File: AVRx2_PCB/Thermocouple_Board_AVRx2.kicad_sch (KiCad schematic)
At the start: 78 parts, among them J6 UPDI-1, Q1 DMN2310U, U11 STS40-CD1B, U12 ADS1246IPWR, U2 ATtiny1604-SS, U3 H11L1, U4 AP2112K-3.3, U5 AP2112K-3.3, U6 TSZ121, U7 MCP1501T-20E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

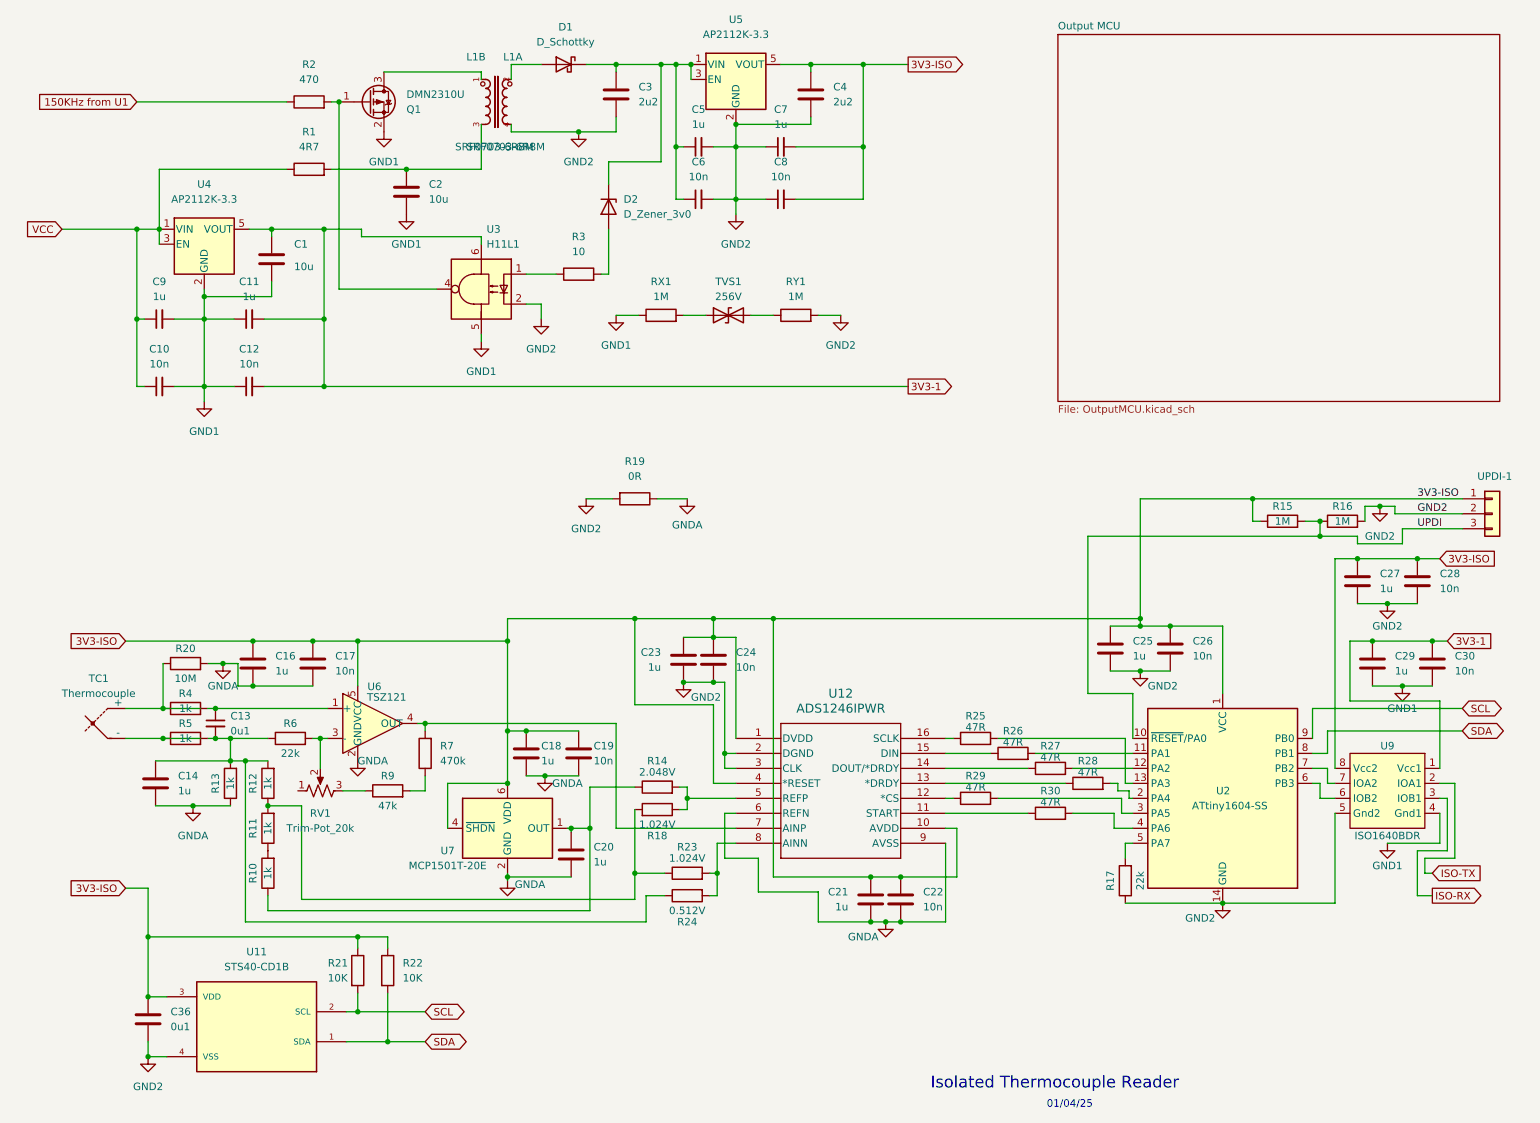
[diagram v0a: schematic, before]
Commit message: Fix a couple of switched traces
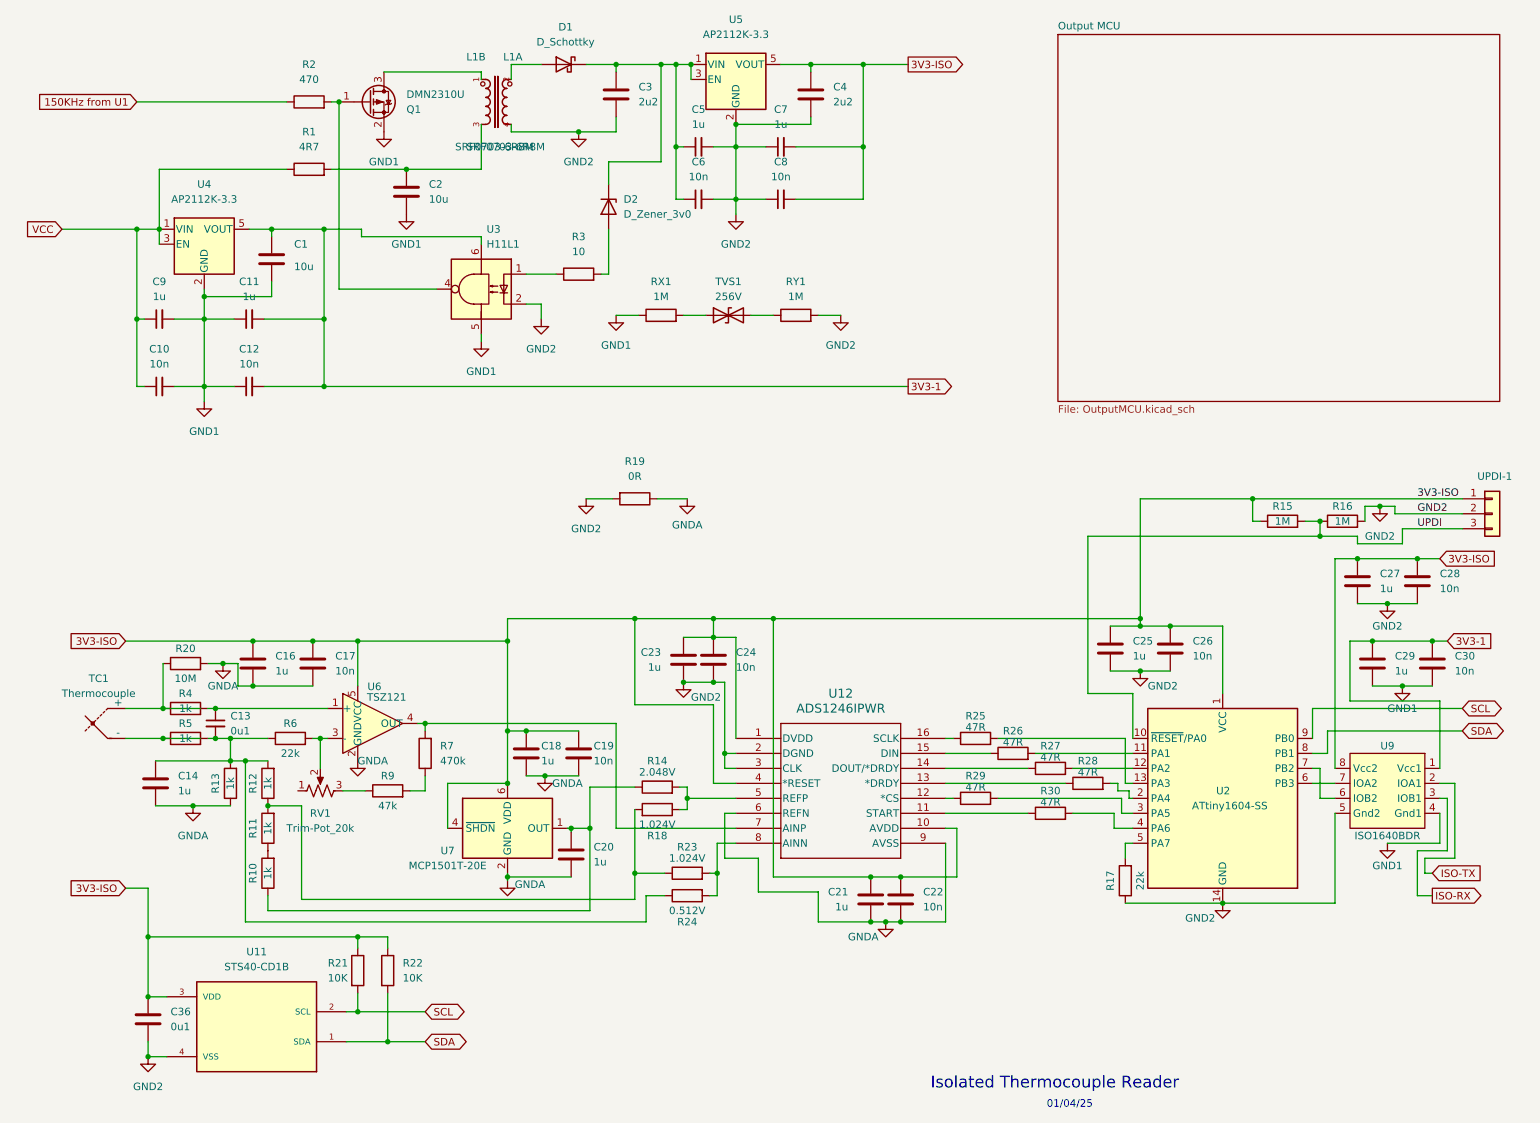
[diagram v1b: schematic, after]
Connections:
- net at U2.6 (PB3): now also U9.7 (IOA2); no longer U9.6 (IOB2)
- net at U2.7 (PB2): now also U9.6 (IOB2); no longer U9.7 (IOA2)

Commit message: Fix crossed traces that were found during prototype testing
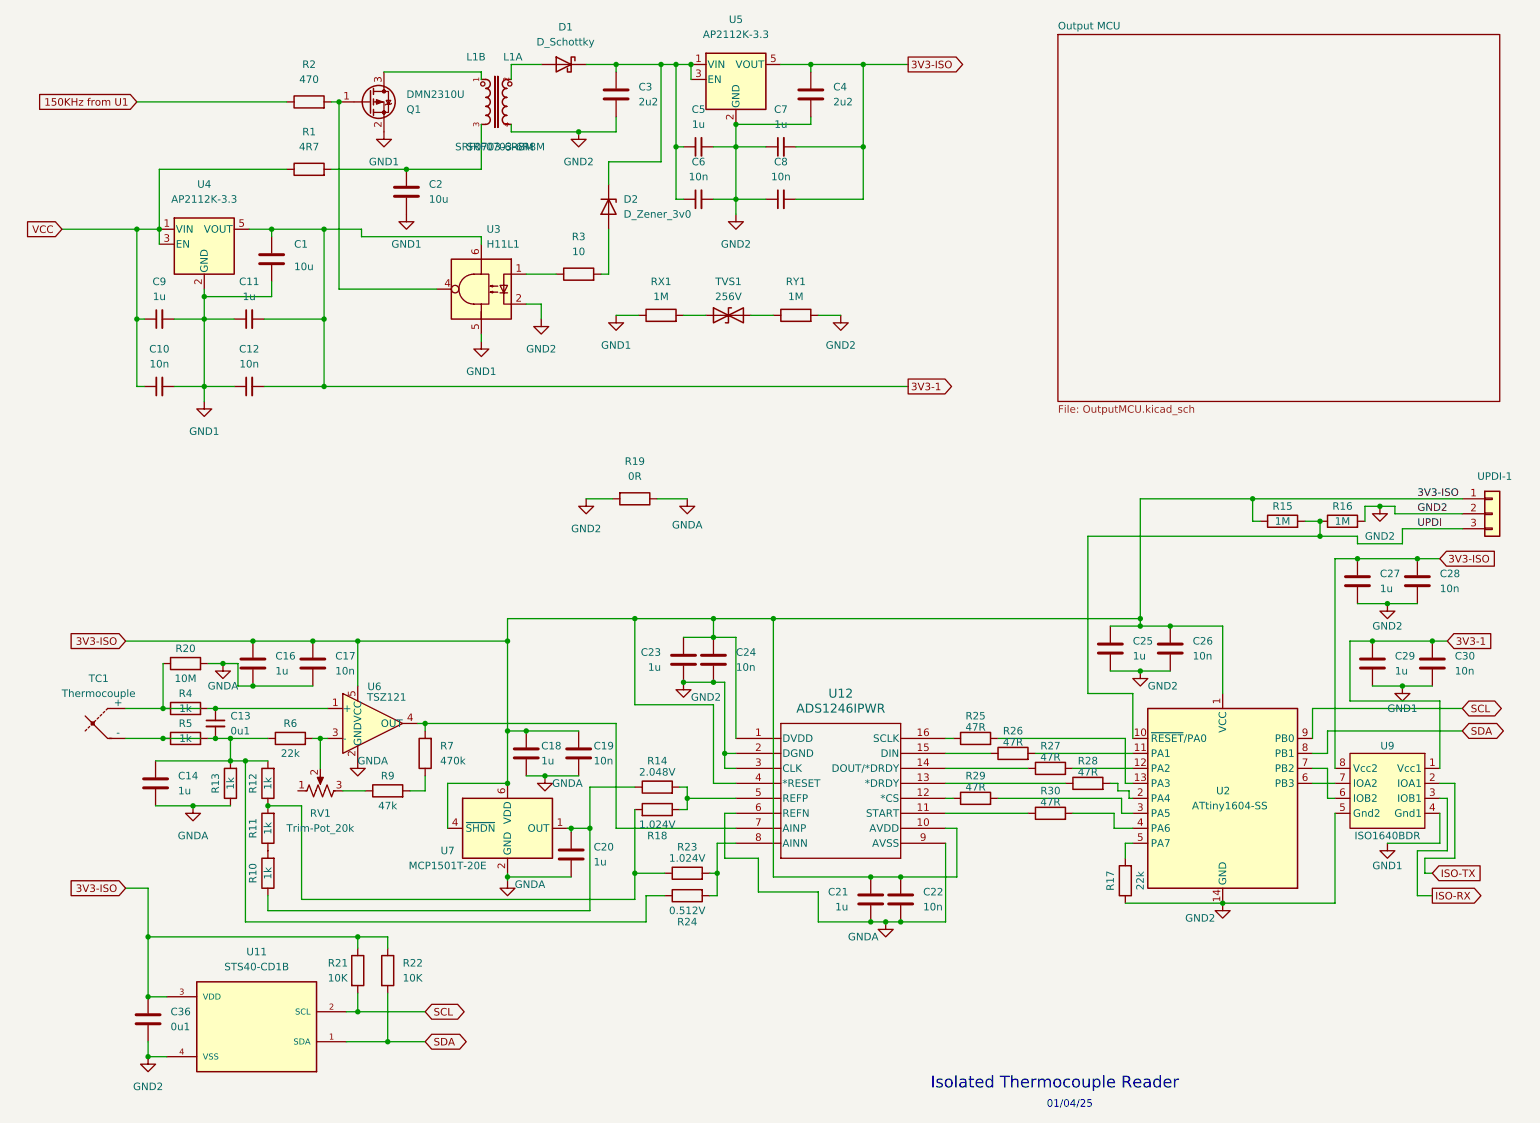
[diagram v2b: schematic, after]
